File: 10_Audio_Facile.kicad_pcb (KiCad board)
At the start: 2 copper layers, 30.5 x 20.3 mm, 18 parts, among them J1 Conn_01x01, J2 Conn_01x01, J3 Conn_01x01, J4 Conn_01x01, J5 Conn_01x01, J6 Conn_01x01, U1 PAM8302AAS

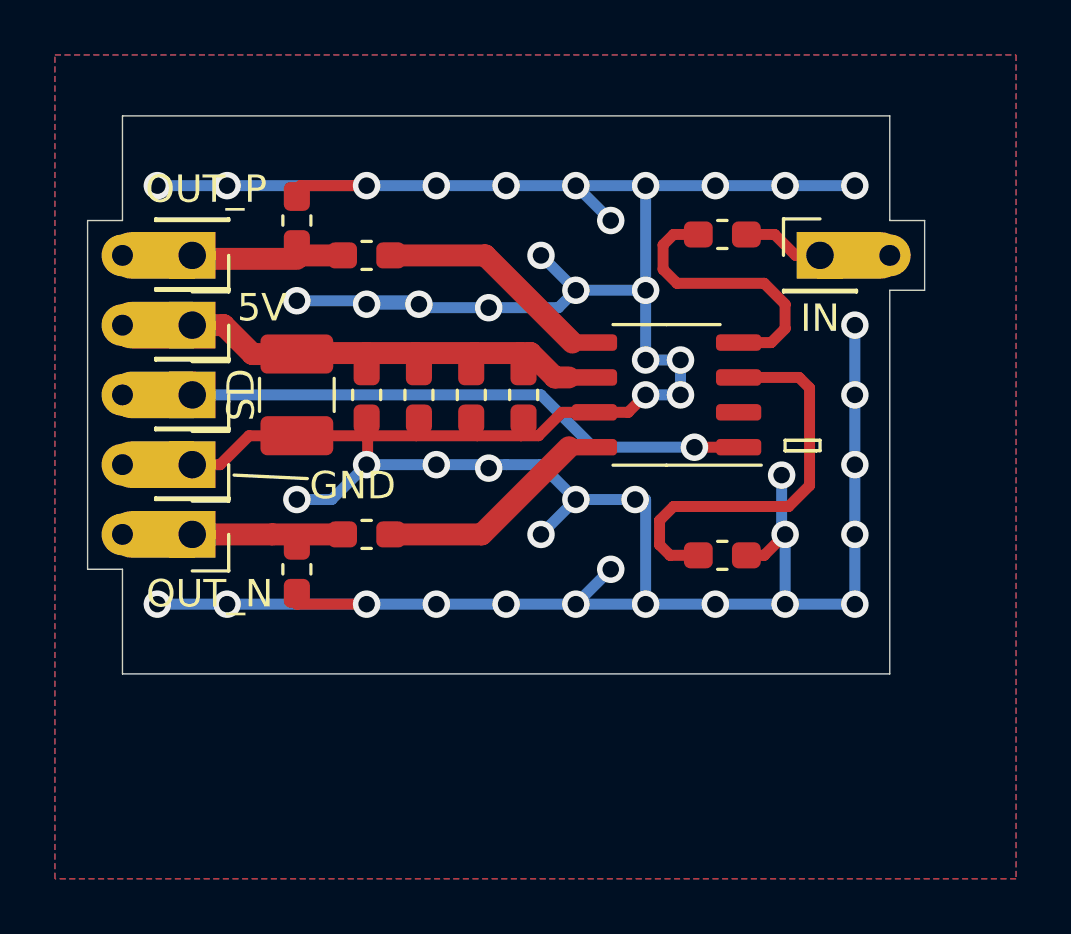
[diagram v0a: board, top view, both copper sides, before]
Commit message: maj kicad v6
maj projet
maj symboles + empreintes
placement plus compact.
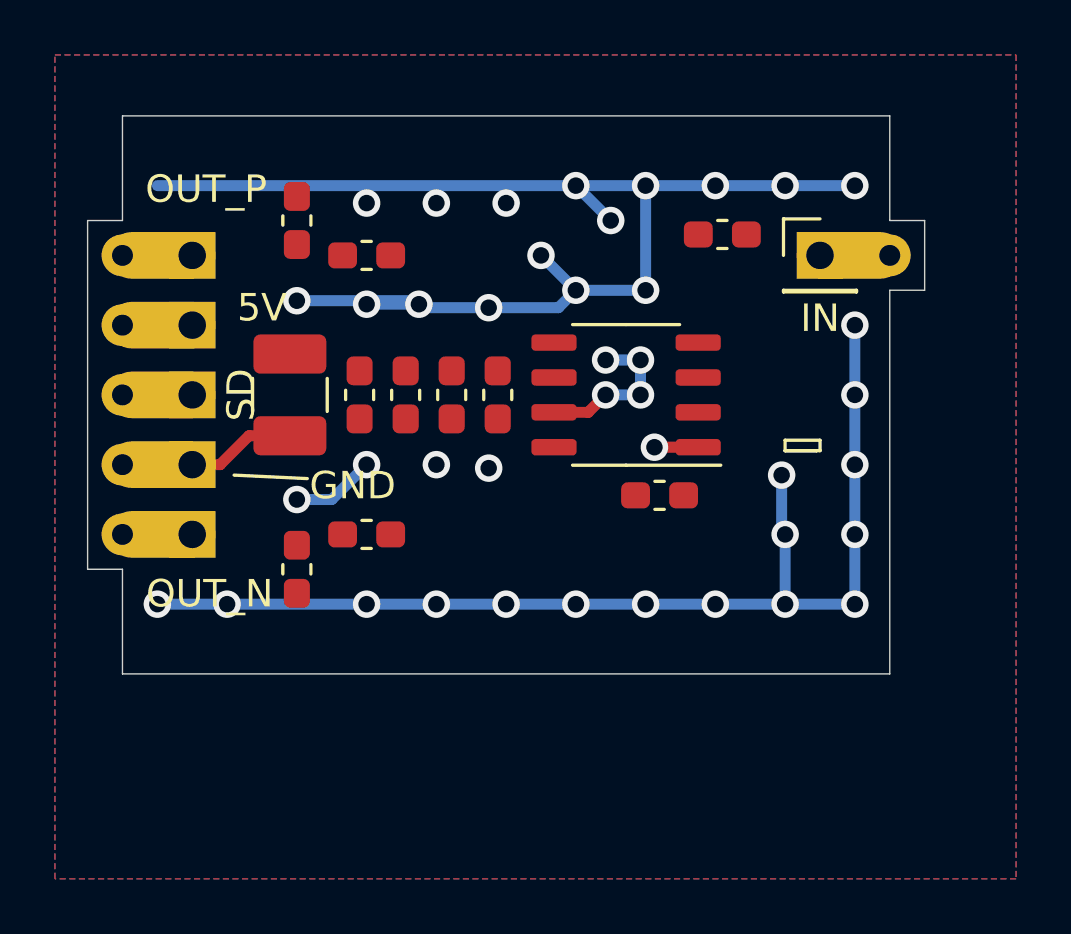
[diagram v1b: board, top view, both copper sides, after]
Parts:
- moved C7 3.16 mm to (121.2, 74.8), turned to 180 degrees
- moved U1 1.47 mm to (119.9, 71.1)
- moved C5 0.94 mm to (115.3, 71.1)
- moved C4 0.71 mm to (113.6, 71.1)
- moved C3 0.48 mm to (111.9, 71.1)
- moved C1 0.25 mm to (107.7, 71.1)
- moved C2 0.25 mm to (110.2, 71.1)
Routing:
- net GND: track 148.2 -> 101.7 mm, vias 46 -> 40
- net SD: track 24.5 -> 1.61 mm
- net 5V: track 22.0 -> 0.05 mm
- net Net-(C7-Pad1): track 14.7 -> 0.00 mm
- net OUT_N: track 10.6 -> 0.00 mm
- net Net-(C8-Pad1): track 10.1 -> 0.00 mm
- net OUT_P: track 9.91 -> 0.00 mm
- net Net-(FB2-Pad1): track 8.74 -> 0.00 mm
- net Net-(FB1-Pad1): track 8.74 -> 0.00 mm
- net IN: track 6.81 -> 0.00 mm
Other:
- net class Default removed
- net class demi-gros removed
- net class gros removed
- board text added: "2023/05/18"
- board text removed: "2021/08/02"
- board text removed: "github.com/ ThierryOrlandi/ 10_Audio_Facile"

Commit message: maj placement routage + fabrication
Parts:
- C1: footprint Capacitor_SMD:C_1210_3225Metric_Pad1.42x2.65mm_HandSolder -> Capacitor_SMD:C_1210_3225Metric
- C2, C3, C4, C5, C6, C7, C8, C9: footprint Capacitor_SMD:C_0603_1608Metric_Pad1.05x0.95mm_HandSolder -> Capacitor_SMD:C_0603_1608Metric
- FB1, FB2: footprint Inductor_SMD:L_0603_1608Metric_Pad1.05x0.95mm_HandSolder -> Inductor_SMD:L_0603_1608Metric
- moved J4 23.0 mm to (104.1, 63.5), turned to 180 degrees
- moved C6 5.80 mm to (113.7, 65.8), turned to 0 degrees
- moved C9 3.86 mm to (111.8, 76.8), turned to 180 degrees
- moved FB1 3.47 mm to (113.7, 67.4)
- moved C8 3.20 mm to (120.3, 64.9), turned to 180 degrees
- moved FB2 1.80 mm to (111.8, 74.9)
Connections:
- U1 pad 2: Net-(U1-Pad2) -> unconnected-(U1-Pad2)
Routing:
- net GND: track 101.7 -> 27.2 mm, vias 40 -> 31
- net 5V: track 0.05 -> 18.7 mm
- net SD: track 1.61 -> 19.2 mm
- net IN: track 0.00 -> 15.8 mm
- net OUT_P: track 0.00 -> 11.1 mm
- net OUT_N: track 0.00 -> 9.36 mm
- net Net-(C8-Pad1): track 0.00 -> 6.79 mm
- net Net-(C7-Pad1): track 0.00 -> 6.62 mm
- net Net-(FB2-Pad1): track 0.00 -> 5.47 mm
- net Net-(FB1-Pad1): track 0.00 -> 4.03 mm
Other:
- board size 30.5 x 20.3 mm -> 22.9 x 16.5 mm
- board text added: "2023/05/19"
- board text added: "Audio_Facile"
- board text removed: "2023/05/18"

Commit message: ajout in+
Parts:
- removed C5: 220pF, Capacitor_SMD:C_0603_1608Metric
- added J7: Conn_01x01, Chimere_mods:Castellated_conn, F.Cu at (104.1, 66.0)
- moved C7 10.5 mm to (118.1, 64.8)
- moved J5 5.08 mm to (104.1, 61.0)
- moved C8 2.80 mm to (118.1, 66.7)
- moved J2 2.54 mm to (104.1, 73.7)
- moved J3 2.54 mm to (104.1, 71.1)
- moved C6 1.73 mm to (112.0, 66.3)
- moved FB1 1.73 mm to (112.0, 67.9)
- moved U1 1.68 mm to (118.3, 71.1)
- moved C9 0.65 mm to (111.9, 76.2)
- moved FB2 0.40 mm to (111.9, 74.5)
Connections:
- net IN renamed IN-
- C7 pad 2: GND -> IN+
- J2 pad 1: SD -> GND
- J3 pad 1: GND -> SD
- J5 pad 1: OUT_P -> IN+
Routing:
- net GND: track 27.2 -> 85.7 mm, vias 31 -> 30
- net IN+: track 0.00 -> 14.8 mm
- net Net-(C8-Pad1): track 6.79 -> 4.17 mm
- net 5V: track 18.7 -> 16.1 mm
- net Net-(C7-Pad1): track 6.62 -> 8.62 mm, vias 0 -> 2
- net Net-(FB2-Pad1): track 5.47 -> 3.59 mm
- net SD: track 19.2 -> 17.5 mm
- net IN-: track 15.8 -> 14.5 mm
- net OUT_P: track 11.1 -> 10.1 mm
- net Net-(FB1-Pad1): track 4.03 -> 3.36 mm
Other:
- board size 22.9 x 16.5 mm -> 22.9 x 17.8 mm
- board text added: "2023/05/26"
- board text added: "IN+"
- board text added: "IN-"
- board text removed: "2023/05/19"
- board text removed: "IN"
